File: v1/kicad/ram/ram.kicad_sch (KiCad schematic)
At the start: 3 parts, among them IC1 AS6C6264-55PCN, U1 LNCPU Type A Connector, U2 74LS32

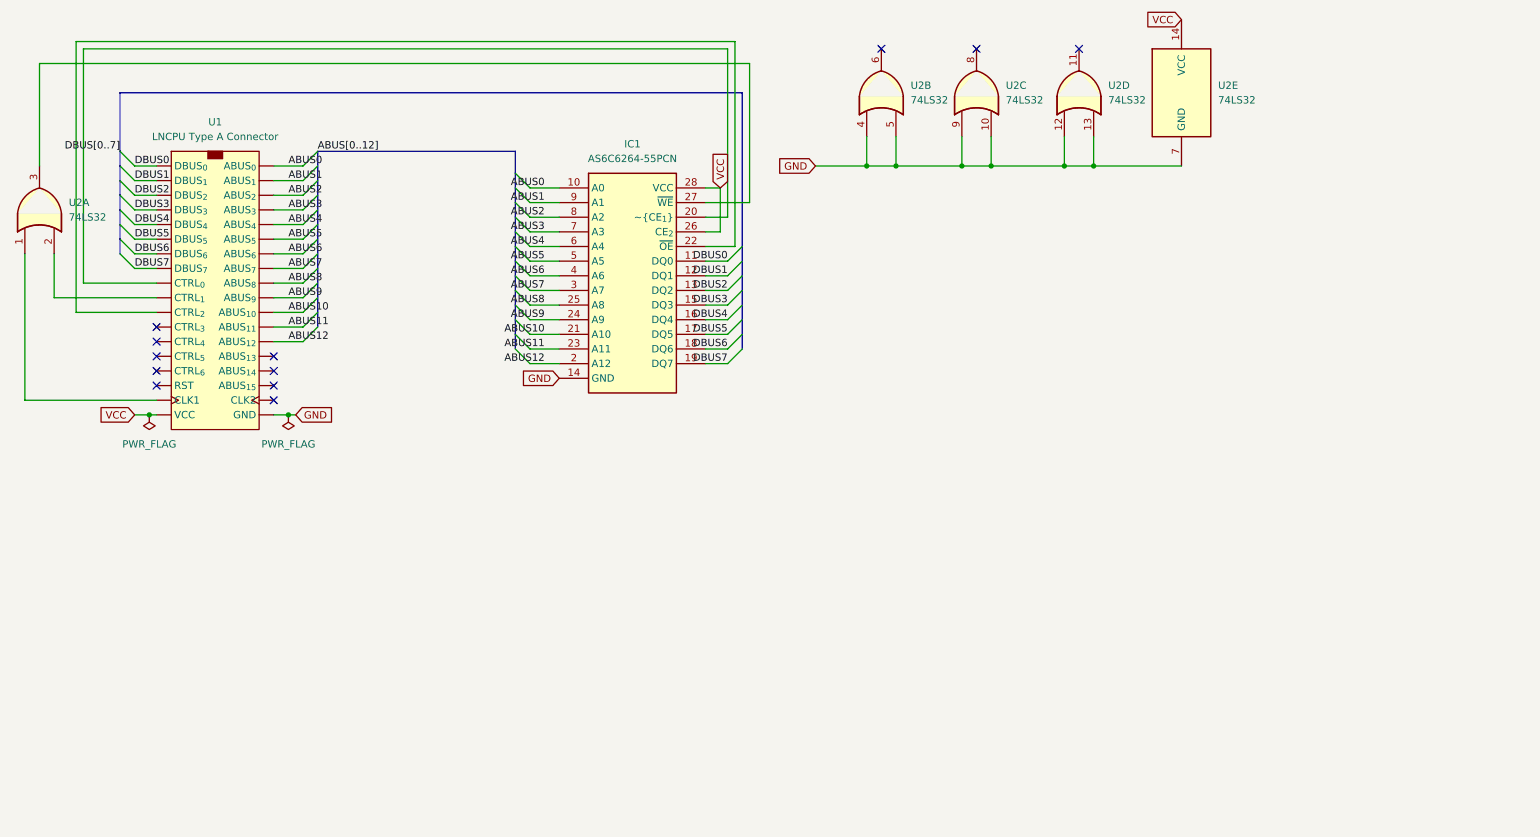
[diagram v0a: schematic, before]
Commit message: readapt designs for BR, SP, SR, ALU
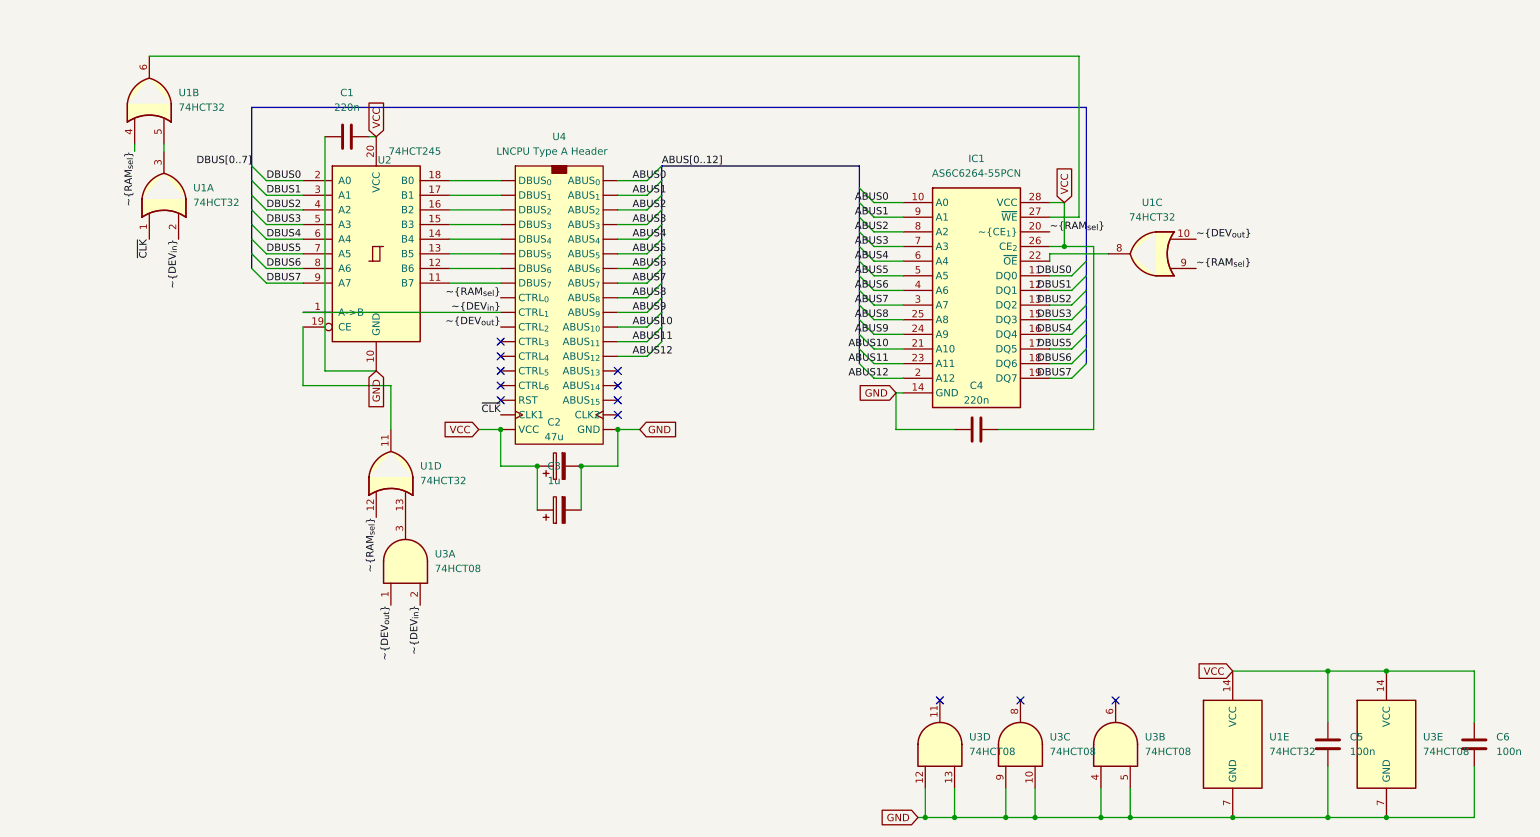
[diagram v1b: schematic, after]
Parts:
- removed unit 4 of U2
- removed unit 2 of U2
- removed unit 3 of U2
- added C1, C4: 220n, Capacitor_THT:C_Disc_D5.0mm_W2.5mm_P2.50mm, symbol Device:C
- added C2: 47u, Capacitor_THT:CP_Radial_D5.0mm_P2.50mm, symbol Device:C_Polarized
- added C3: 1u, lncpu:CP_Radial_D4.0mm_P2.00mm-Large-Holes, symbol Device:C_Polarized
- added C5, C6: 100n, Capacitor_THT:C_Disc_D5.0mm_W2.5mm_P2.50mm, symbol Device:C
- added unit 3 of U1
- added unit 2 of U1
- added unit 4 of U1
- added U2: 74HCT245, Package_DIP:DIP-20_W7.62mm_LongPads, symbol 74xx:74HC245
- added U3: 74HCT08, Package_DIP:DIP-14_W7.62mm_LongPads, symbol 74xx:74LS08
- IC1: symbol AS6C6264-55PCN:AS6C6264-55PCN -> AS6C6264:AS6C6264-55PCN
- U1: renamed from U2; value 74LS32 -> 74HCT32
- U4: renamed from U1; value LNCPU Type A Connector -> LNCPU Type A Header; symbol lncpu:LNCPU_Type_A_Connector -> lncpu:LNCPU_Type_A_Header
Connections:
- net DBUS0: now also U2.2 (A0); no longer U4.19 (DBUS_{0})
- net DBUS1: now also U2.3 (A1); no longer U4.21 (DBUS_{1})
- net DBUS2: now also U2.4 (A2); no longer U4.23 (DBUS_{2})
- net DBUS3: now also U2.5 (A3); no longer U4.25 (DBUS_{3})
- net DBUS4: now also U2.6 (A4); no longer U4.27 (DBUS_{4})
- net DBUS5: now also U2.7 (A5); no longer U4.29 (DBUS_{5})
- net DBUS6: now also U2.8 (A6); no longer U4.31 (DBUS_{6})
- net DBUS7: now also U2.9 (A7); no longer U4.33 (DBUS_{7})
- net GND: now also C1.1, C2.2, C3.2, C4.1, C5.1, C6.1, U2.10 (GND), U3.10, U3.12, U3.13, U3.4, U3.5, U3.7 (GND), U3.9
- net VCC: now also C1.2, C2.1, C3.1, C4.2, C5.2, C6.2, U2.20 (VCC), U3.14 (VCC)
- net ~{CLK}: now reaches U1.1, U4.35 (CLK1)
- net ~{DEV_{in}}: now reaches U1.2, U4.5 (CTRL_{1})
- net ~{DEV_{in}}: now also U2.1 (A->B), U3.2
- net at U1.3: now also U1.5; no longer IC1.27 (~{WE})
- net ~{RAM_{sel}}: now reaches IC1.20 (~{CE_{1}}), U4.3 (CTRL_{0})
- net ~{RAM_{sel}}: now also U1.12, U1.4, U1.9
- net at IC1.22 (~{OE}): now also U1.8; no longer U4.7 (CTRL_{2})
- new net: U2.11 (B7), U4.33 (DBUS_{7})
- new net: U2.12 (B6), U4.31 (DBUS_{6})
- new net: U2.13 (B5), U4.29 (DBUS_{5})
- new net: U2.14 (B4), U4.27 (DBUS_{4})
- new net: U2.15 (B3), U4.25 (DBUS_{3})
- new net: U2.16 (B2), U4.23 (DBUS_{2})
- new net: U2.17 (B1), U4.21 (DBUS_{1})
- new net: U2.18 (B0), U4.19 (DBUS_{0})
- new net: U1.11, U2.19 (CE)
- new net: IC1.27 (~{WE}), U1.6
- new net: U1.13, U3.3
- new net ~{DEV_{out}}: U1.10, U3.1, U4.7 (CTRL_{2})
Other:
- moved on the sheet: IC1, U1A, U1E, U4
